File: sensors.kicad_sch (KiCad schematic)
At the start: 7 parts, among them U6 ICM-42688-P, U7 ICP-10111

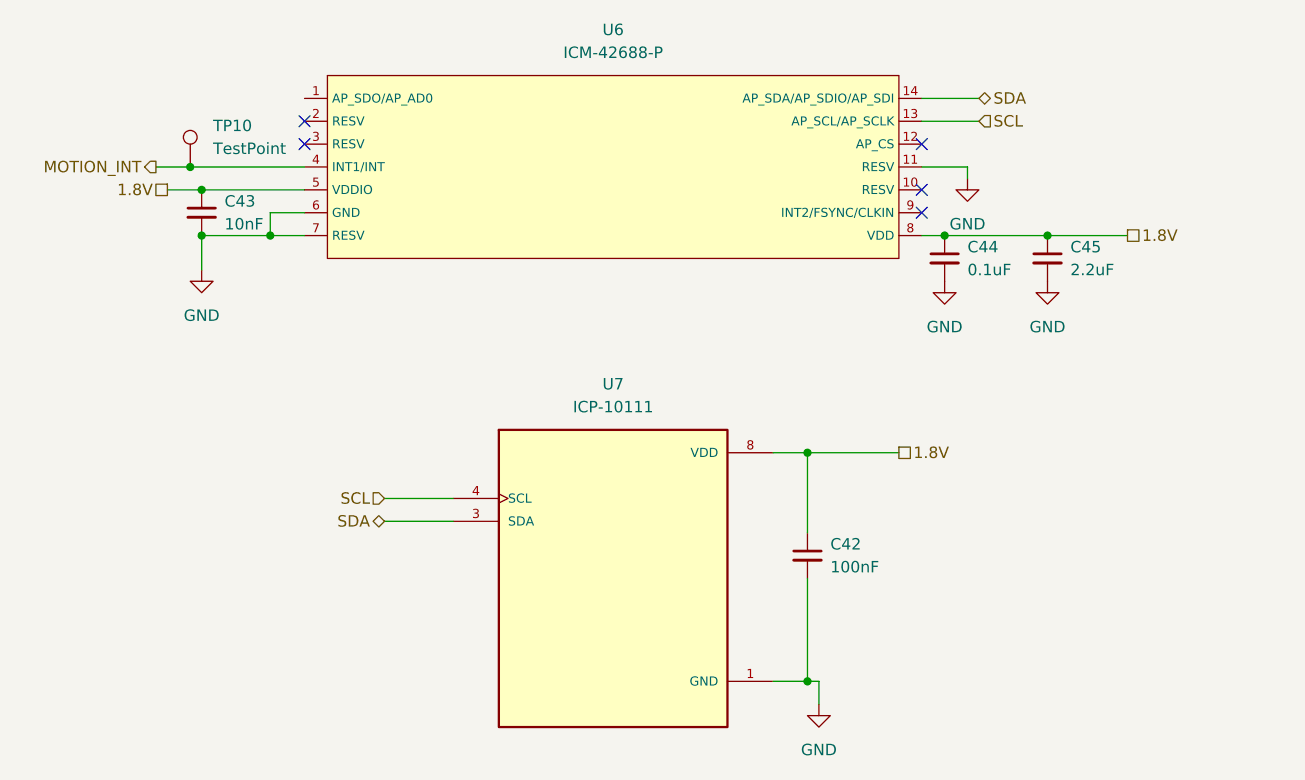
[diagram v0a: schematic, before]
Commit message: route PMIC
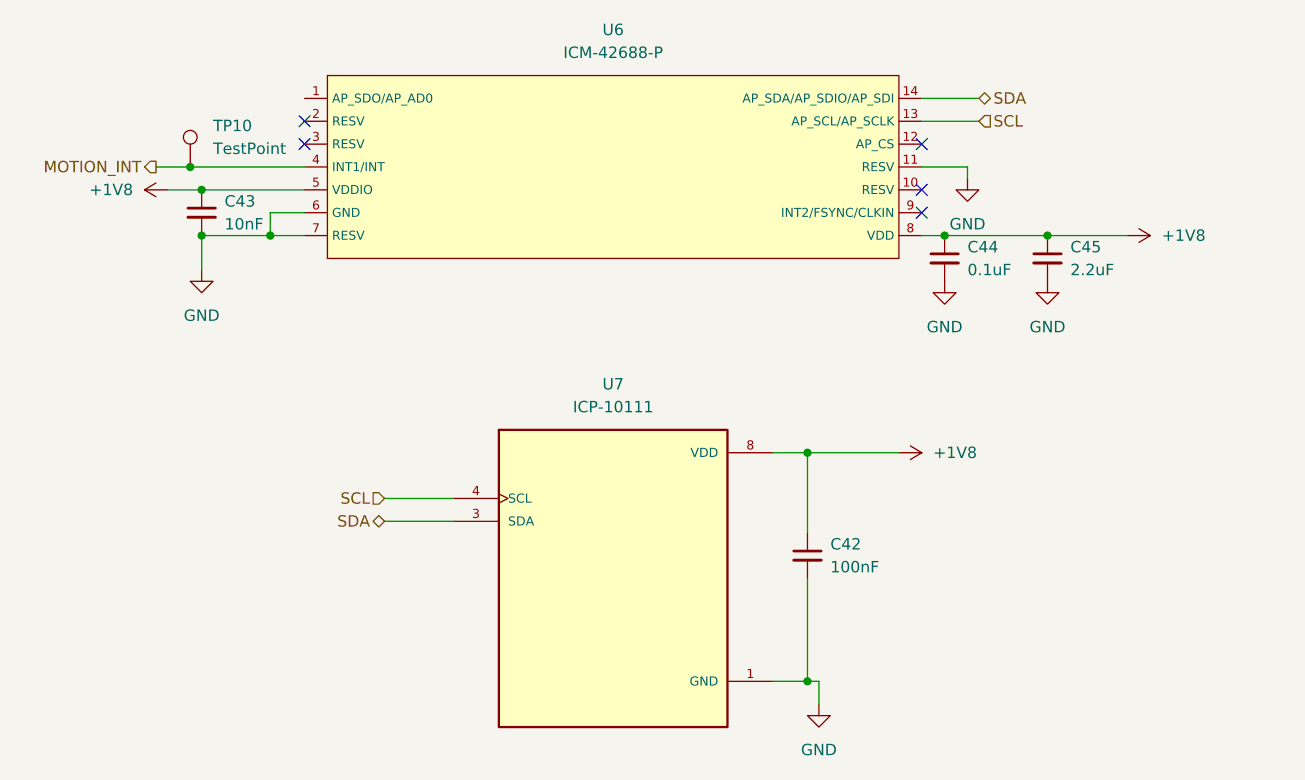
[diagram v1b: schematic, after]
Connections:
- net 1.8V renamed +1V8
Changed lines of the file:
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@@
 		)
 	)
-	(hierarchical_label "1.8V"
-		(shape passive)
-		(at 114.3 76.2 0)
+	(hierarchical_label "SCL"
+		(shape input)
+		(at 57.15 81.28 180)
 		(fields_autoplaced yes)
 		(effects
@@
 				(size 1.27 1.27)
 			)
-			(justify left)
-		)
-	)
-	(hierarchical_label "SCL"
-		(shape input)
-		(at 57.15 81.28 180)
+			(justify right)
+		)
+	)
+	(hierarchical_label "MOTION_INT"
+		(shape output)
+		(at 31.75 44.45 180)
 		(fields_autoplaced yes)
 		(effects
@@
 		)
 	)
-	(hierarchical_label "1.8V"
-		(shape passive)
-		(at 33.02 46.99 180)
+	(hierarchical_label "SDA"
+		(shape bidirectional)
+		(at 123.19 36.83 0)
 		(fields_autoplaced yes)
 		(effects
@@
 				(size 1.27 1.27)
 			)
-			(justify right)
-		)
-	)
-	(hierarchical_label "MOTION_INT"
-		(shape output)
-		(at 31.75 44.45 180)
-		(fields_autoplaced yes)
-		(effects
-			(font
-				(size 1.27 1.27)
-			)
-			(justify right)
-		)
-	)
-	(hierarchical_label "SDA"
-		(shape bidirectional)
-		(at 123.19 36.83 0)
-		(fields_autoplaced yes)
-		(effects
-			(font
-				(size 1.27 1.27)
-			)
-			(justify left)
-		)
-	)
-	(hierarchical_label "1.8V"
-		(shape passive)
-		(at 139.7 52.07 0)
-		(fields_autoplaced yes)
-		(effects
-			(font
-				(size 1.27 1.27)
-			)
 			(justify left)
 		)
@@
 	)
 	(symbol
+		(lib_id "power:+1V8")
+		(at 139.7 52.07 270)
+		(unit 1)
+		(exclude_from_sim no)
+		(in_bom yes)
+		(on_board yes)
+		(dnp no)
+		(fields_autoplaced yes)
+		(property "Reference" "#PWR076"
+			(at 135.89 52.07 0)
+			(effects
+				(font
+					(size 1.27 1.27)
+				)
+				(hide yes)
+			)
+		)
+		(property "Value" "+1V8"
+			(at 143.51 52.0699 90)
+			(effects
+				(font
+					(size 1.27 1.27)
+				)
+				(justify left)
+			)
+		)
+		(property "Footprint" ""
+			(at 139.7 52.07 0)
+			(effects
+				(font
+					(size 1.27 1.27)
+				)
+				(hide yes)
+			)
+		)
+		(property "Datasheet" ""
+			(at 139.7 52.07 0)
+			(effects
+				(font
+					(size 1.27 1.27)
+				)
+				(hide yes)
+			)
+		)
+		(property "Description" "Power symbol creates a global label with name \"+1V8\""
+			(at 139.7 52.07 0)
+			(effects
+				(font
+					(size 1.27 1.27)
+				)
+				(hide yes)
+			)
+		)
+		(pin "1"
+		)
+		(instances
+			(project ""
+				(path "/110ea5a2-03d6-426d-b79f-fcb4ea6cee9d/7aa00029-f5f2-4535-b444-7e5f9da482b1"
+					(reference "#PWR076")
+					(unit 1)
+				)
+			)
+		)
+	)
+	(symbol
 		(lib_id "Library:ICM-42688-P")
 		(at 82.55 44.45 0)
@@
 					(unit 1)
 				)
+			)
+		)
+	)
+	(symbol
+		(lib_id "power:+1V8")
+		(at 33.02 46.99 90)
+		(unit 1)
+		(exclude_from_sim no)
+		(in_bom yes)
+		(on_board yes)
+		(dnp no)
+		(fields_autoplaced yes)
+		(property "Reference" "#PWR074"
+			(at 36.83 46.99 0)
+			(effects
+				(font
+					(size 1.27 1.27)
+				)
+				(hide yes)
+			)
+		)
+		(property "Value" "+1V8"
+			(at 29.21 46.9899 90)
+			(effects
+				(font
+					(size 1.27 1.27)
+				)
+				(justify left)
+			)
+		)
+		(property "Footprint" ""
+			(at 33.02 46.99 0)
+			(effects
+				(font
+					(size 1.27 1.27)
+				)
+				(hide yes)
+			)
+		)
+		(property "Datasheet" ""
+			(at 33.02 46.99 0)
+			(effects
+				(font
+					(size 1.27 1.27)
+				)
+				(hide yes)
+			)
+		)
+		(property "Description" "Power symbol creates a global label with name \"+1V8\""
+			(at 33.02 46.99 0)
+			(effects
+				(font
+					(size 1.27 1.27)
+				)
+				(hide yes)
+			)
+		)
+		(pin "1"
+		)
+		(instances
+			(project ""
+				(path "/110ea5a2-03d6-426d-b79f-fcb4ea6cee9d/7aa00029-f5f2-4535-b444-7e5f9da482b1"
+					(reference "#PWR074")
+					(unit 1)
+				)
+			)
+		)
+	)
+	(symbol
+		(lib_id "power:+1V8")
+		(at 114.3 76.2 270)
+		(unit 1)
+		(exclude_from_sim no)
+		(in_bom yes)
+		(on_board yes)
+		(dnp no)
+		(fields_autoplaced yes)
+		(property "Reference" "#PWR075"
+			(at 110.49 76.2 0)
+			(effects
+				(font
+					(size 1.27 1.27)
+				)
+				(hide yes)
+			)
+		)
+		(property "Value" "+1V8"
+			(at 118.11 76.1999 90)
+			(effects
+				(font
+					(size 1.27 1.27)
+				)
+				(justify left)
+			)
+		)
+		(property "Footprint" ""
+			(at 114.3 76.2 0)
+			(effects
+				(font
+					(size 1.27 1.27)
+				)
+				(hide yes)
+			)
+		)
+		(property "Datasheet" ""
+			(at 114.3 76.2 0)
+			(effects
+				(font
+					(size 1.27 1.27)
+				)
+				(hide yes)
+			)
+		)
+		(property "Description" "Power symbol creates a global label with name \"+1V8\""
+			(at 114.3 76.2 0)
+			(effects
+				(font
+					(size 1.27 1.27)
+				)
+				(hide yes)
+			)
+		)
+		(pin "1"
+		)
+		(instances
+			(project ""
+				(path "/110ea5a2-03d6-426d-b79f-fcb4ea6cee9d/7aa00029-f5f2-4535-b444-7e5f9da482b1"
+					(reference "#PWR075")
+					(unit 1)
+				)

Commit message: stuff
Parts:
- added U11: IST8308, Package_LGA:LGA-16_3x3mm_P0.5mm, symbol Sensor_Magnetic:IST8308
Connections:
- new net: U11.11 (VSS), U11.9 (VSS)
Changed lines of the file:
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@@
+	)
+	(symbol
+		(lib_id "Sensor_Magnetic:IST8308")
+		(at 146.05 87.63 0)
+		(unit 1)
+		(exclude_from_sim no)
+		(in_bom yes)
+		(on_board yes)
+		(dnp no)
+		(fields_autoplaced yes)
+		(property "Reference" "U11"
+			(at 148.2441 100.33 0)
+			(effects
+				(font
+					(size 1.27 1.27)
+				)
+				(justify left)
+			)
+		)
+		(property "Value" "IST8308"
+			(at 148.2441 102.87 0)
+			(effects
+				(font
+					(size 1.27 1.27)
+				)
+				(justify left)
+			)
+		)
+		(property "Footprint" "Package_LGA:LGA-16_3x3mm_P0.5mm"
+			(at 146.05 87.63 0)
+			(effects
+				(font
+					(size 1.27 1.27)
+				)
+				(hide yes)
+			)
+		)
+		(property "Datasheet" "http://www.isentek.com/en/dlf.php?file=../ISENTEK/(201703-20)IST8308%20Datasheet%20v1.0_brief.pdf"
+			(at 146.05 87.63 0)
+			(effects
+				(font
+					(size 1.27 1.27)
+				)
+				(hide yes)
+			)
+		)
+		(property "Description" "3D Magnetometer, High Sensitivity, I2C Interface, LGA-16"
+			(at 146.05 87.63 0)
+			(effects
+				(font
+					(size 1.27 1.27)
+				)
+				(hide yes)
+			)
+		)
+		(pin "4"
+		)
+		(pin "9"
+		)
+		(pin "10"
+		)
+		(pin "8"
+		)
+		(pin "5"
+		)
+		(pin "1"
+		)
+		(pin "13"
+		)
+		(pin "6"
+		)
+		(pin "16"
+		)
+		(pin "7"
+		)
+		(pin "11"
+		)
+		(pin "2"
+		)
+		(pin "14"
+		)
+		(pin "3"
+		)
+		(pin "12"
+		)
+		(pin "15"
+		)
+		(instances
+			(project ""
+				(path "/110ea5a2-03d6-426d-b79f-fcb4ea6cee9d/7aa00029-f5f2-4535-b444-7e5f9da482b1"
+					(reference "U11")
+					(unit 1)
+				)
+			)
+		)
 	)
 	(symbol
